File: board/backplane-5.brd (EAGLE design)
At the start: 100 x 100 mm, 155 parts, among them CN1 RJ45JACK90, CN2 4PINCONNFEMALE-1.6, CN3 4PINCONNFEMALE-1.6, CN4 4PINCONNFEMALE-1.6, CN5 4PINCONNFEMALE-1.6, CN6 4PINCONNFEMALE-1.6, U1 AMS1117-5.0, U10 RT9193, U11 KSZ9897, U12 KSZ8081MLX, U13 STM32F217-100, U2 AMS1117-5.0, U3 AMS1117-5.0, U4 AMS1117-5.0, U5 AMS1117-5.0, U6 AMS1117-2.5, U7 AMS1117-1.2, U8 RT9193, U9 AMS1117-5.0, Y1 25MHz, Y2 25MHz, Y3 25MHz

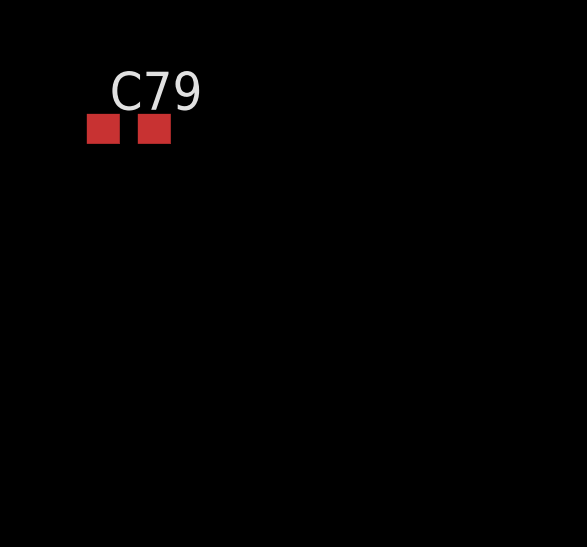
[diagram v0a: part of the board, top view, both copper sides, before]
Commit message: Added VCAP capacitors
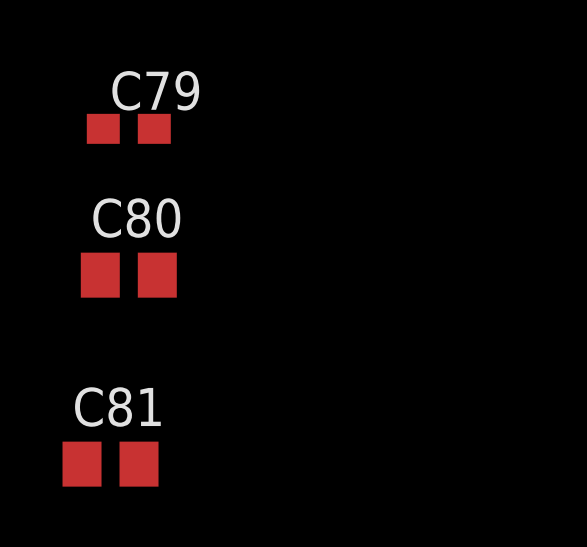
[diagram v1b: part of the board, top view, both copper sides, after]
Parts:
- added C80, C81: 2.2uF, tuetuopay:0805
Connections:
- new net N$34: C80.1, U13.73
- new net N$35: C81.1, U13.49
- net GND: now also C80.2, C81.2
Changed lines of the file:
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@@
 <element name="C78" library="tuetuopay" package="0603" value="10nF" x="-151.1808" y="-580.7456"/>
 <element name="C79" library="tuetuopay" package="0603" value="10nF" x="-151.1808" y="-585.6224"/>
+<element name="C80" library="tuetuopay" package="0805" value="2.2uF" x="-151.1808" y="-590.4992"/>
+<element name="C81" library="tuetuopay" package="0805" value="2.2uF" x="-151.7904" y="-596.7984"/>
 </elements>
 <signals>
@@
 <contactref element="C69" pad="2"/>
 <contactref element="C71" pad="2"/>
-<contactref element="U13" pad="10"/>
-<contactref element="U13" pad="20"/>
-<contactref element="U13" pad="27"/>
-<contactref element="U13" pad="74"/>
 <contactref element="C72" pad="2"/>
 <contactref element="C79" pad="2"/>
@@
 <contactref element="C77" pad="2"/>
 <contactref element="C78" pad="2"/>
+<contactref element="C81" pad="2"/>
+<contactref element="U13" pad="10"/>
+<contactref element="U13" pad="20"/>
+<contactref element="U13" pad="27"/>
+<contactref element="U13" pad="74"/>
+<contactref element="C80" pad="2"/>
 <wire x1="-106.26" y1="-387.35" x2="-106.26" y2="-400.05" width="0" layer="19" extent="1-1"/>
 <wire x1="-106.26" y1="-374.65" x2="-106.26" y2="-387.35" width="0" layer="19" extent="1-1"/>
@@
 <wire x1="-150.3308" y1="-580.7456" x2="-150.3308" y2="-575.8688" width="0" layer="19" extent="1-1"/>
 <wire x1="-150.3308" y1="-585.6224" x2="-150.3308" y2="-580.7456" width="0" layer="19" extent="1-1"/>
+<wire x1="-150.2308" y1="-590.4992" x2="-150.3308" y2="-585.6224" width="0" layer="19" extent="1-1"/>
+<wire x1="-150.8404" y1="-596.7984" x2="-150.2308" y2="-590.4992" width="0" layer="19" extent="1-1"/>
 <wire x1="-76.62" y1="-128.27" x2="-84.24" y2="-219.71" width="0" layer="19" extent="1-1"/>
 <wire x1="12.44" y1="5.83" x2="-76.62" y2="-128.27" width="0" layer="19" extent="1-1"/>
@@
 <wire x1="-137.8792" y1="-534.038" x2="-152.0308" y2="-546.608" width="0" layer="19" extent="1-1"/>
 </signal>
+<signal name="N$34">
+<contactref element="U13" pad="73"/>
+<contactref element="C80" pad="1"/>
+<wire x1="-143.3792" y1="-518.538" x2="-152.1308" y2="-590.4992" width="0" layer="19" extent="1-1"/>
+</signal>
+<signal name="N$35">
+<contactref element="U13" pad="49"/>
+<contactref element="C81" pad="1"/>
+<wire x1="-130.6292" y1="-520.788" x2="-152.7404" y2="-596.7984" width="0" layer="19" extent="1-1"/>
+</signal>
 </signals>

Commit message: Added switch <-> stm32 rmii in schematic
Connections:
- new net STM32-ETH-CRSDV: U11.P$76, U13.32
- new net STM32-ETH-REFCLK: U11.P$66, U13.24
- new net STM32-ETH-RXD0: U11.P$83, U13.33
- new net STM32-ETH-RXD1: U11.P$82, U13.34
- new net STM32-ETH-TXD0: U11.P$73, U13.51
- new net STM32-ETH-TXD1: U11.P$72, U13.52
- new net STM32-ETH-TXEN: U11.P$67, U13.48
- net MDC: now also U13.16
- net MDIO: now also U13.25
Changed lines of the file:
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@@
 <contactref element="U11" pad="P$101"/>
 <contactref element="JP1" pad="2"/>
+<contactref element="U13" pad="16"/>
+<wire x1="-137.16" y1="-509.27" x2="-136.8792" y2="-534.038" width="0" layer="19" extent="1-1"/>
 <wire x1="31.9492" y1="22.5724" x2="-137.16" y2="-509.27" width="0" layer="19" extent="1-1"/>
 <wire x1="66.528" y1="24.6608" x2="31.9492" y2="22.5724" width="0" layer="19" extent="1-1"/>
@@
 <wire x1="31.4492" y1="22.5724" x2="31.4492" y2="20.2008" width="0.2032" layer="1"/>
 <wire x1="31.4492" y1="20.2008" x2="31.6992" y2="19.9508" width="0.2032" layer="1"/>
+<contactref element="U13" pad="25"/>
+<wire x1="-139.7" y1="-509.27" x2="-132.3792" y2="-534.038" width="0" layer="19" extent="1-1"/>
 <wire x1="31.6992" y1="19.9508" x2="-139.7" y2="-509.27" width="0" layer="19" extent="1-1"/>
 <wire x1="66.528" y1="23.4608" x2="31.6992" y2="19.9508" width="0" layer="19" extent="1-1"/>
@@
 <wire x1="-130.6292" y1="-520.788" x2="-152.7404" y2="-596.7984" width="0" layer="19" extent="1-1"/>
 </signal>
+<signal name="STM32-ETH-REFCLK">
+<contactref element="U13" pad="24"/>
+<contactref element="U11" pad="P$66"/>
+<wire x1="53.128" y1="22.0608" x2="-132.8792" y2="-534.038" width="0" layer="19" extent="1-1"/>
+</signal>
+<signal name="STM32-ETH-CRSDV">
+<contactref element="U13" pad="32"/>
+<contactref element="U11" pad="P$76"/>
+<wire x1="57.128" y1="22.0608" x2="-130.6292" y2="-529.288" width="0" layer="19" extent="1-1"/>
+</signal>
+<signal name="STM32-ETH-RXD0">
+<contactref element="U13" pad="33"/>
+<contactref element="U11" pad="P$83"/>
+<wire x1="59.928" y1="22.0608" x2="-130.6292" y2="-528.788" width="0" layer="19" extent="1-1"/>
+</signal>
+<signal name="STM32-ETH-RXD1">
+<contactref element="U13" pad="34"/>
+<contactref element="U11" pad="P$82"/>
+<wire x1="59.528" y1="22.0608" x2="-130.6292" y2="-528.288" width="0" layer="19" extent="1-1"/>
+</signal>
+<signal name="STM32-ETH-TXEN">
+<contactref element="U13" pad="48"/>
+<contactref element="U11" pad="P$67"/>
+<wire x1="53.528" y1="22.0608" x2="-130.6292" y2="-521.288" width="0" layer="19" extent="1-1"/>
+</signal>
+<signal name="STM32-ETH-TXD0">
+<contactref element="U13" pad="51"/>
+<contactref element="U11" pad="P$73"/>
+<wire x1="55.928" y1="22.0608" x2="-132.3792" y2="-518.538" width="0" layer="19" extent="1-1"/>
+</signal>
+<signal name="STM32-ETH-TXD1">
+<contactref element="U13" pad="52"/>
+<contactref element="U11" pad="P$72"/>
+<wire x1="55.528" y1="22.0608" x2="-132.8792" y2="-518.538" width="0" layer="19" extent="1-1"/>
+</signal>
 </signals>

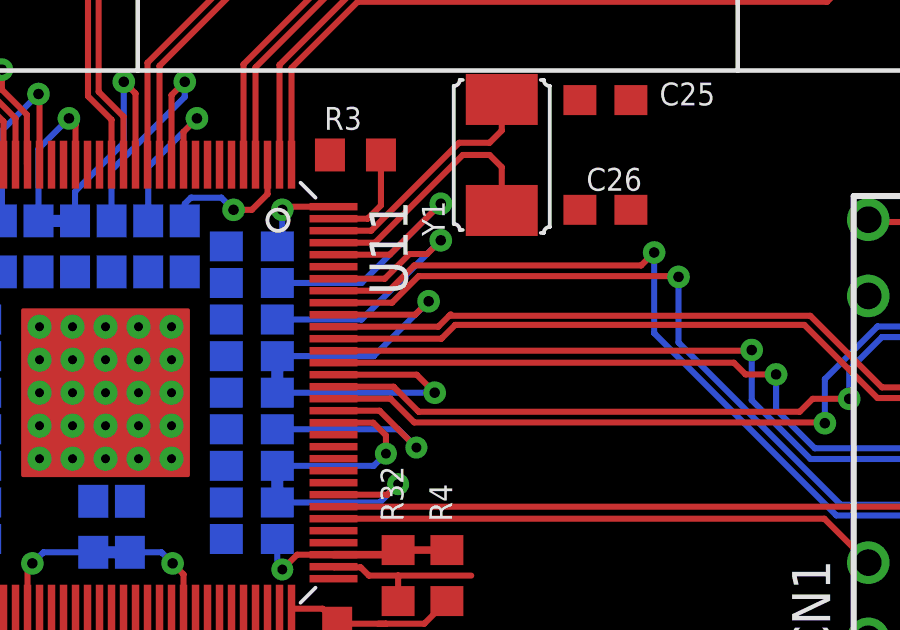
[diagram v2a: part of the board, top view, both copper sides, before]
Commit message: Added the REFCLK source for switch <-> stm
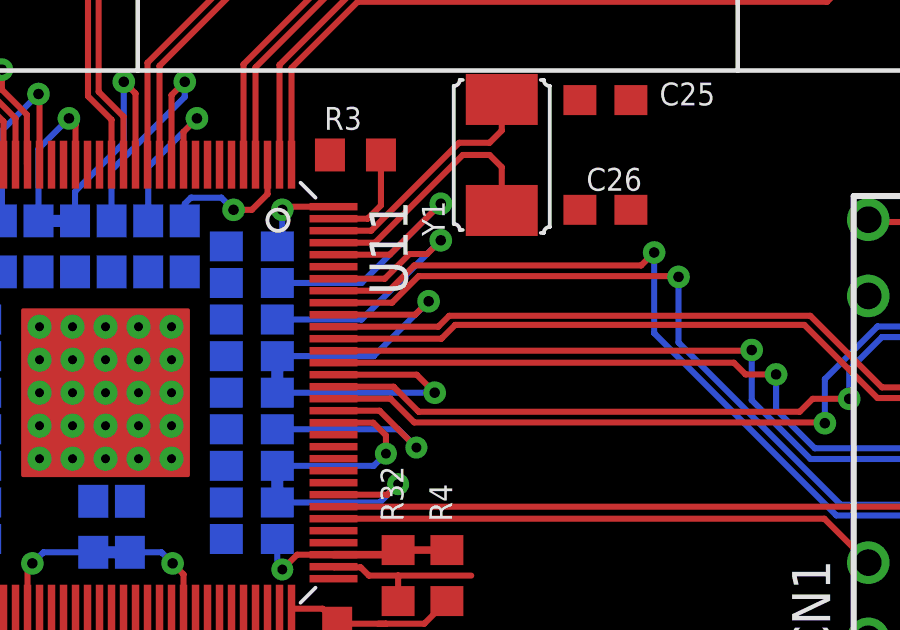
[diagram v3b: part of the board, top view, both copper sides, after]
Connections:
- net STM32-ETH-REFCLK: now also U13.67
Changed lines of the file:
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@@
 <layer number="27" name="tValues" color="7" fill="1" visible="yes" active="yes"/>
 <layer number="28" name="bValues" color="7" fill="1" visible="yes" active="yes"/>
-<layer number="29" name="tStop" color="7" fill="3" visible="no" active="yes"/>
-<layer number="30" name="bStop" color="7" fill="6" visible="no" active="yes"/>
+<layer number="29" name="tStop" color="7" fill="3" visible="yes" active="yes"/>
+<layer number="30" name="bStop" color="7" fill="6" visible="yes" active="yes"/>
 <layer number="31" name="tCream" color="7" fill="4" visible="no" active="yes"/>
 <layer number="32" name="bCream" color="7" fill="5" visible="no" active="yes"/>
@@
 <wire x1="33.528" y1="15.8124" x2="-76.07" y2="-123.19" width="0" layer="19" extent="1-1"/>
 <wire x1="35.1536" y1="15.8124" x2="33.528" y2="15.8124" width="0" layer="19" extent="1-1"/>
+<wire x1="31.6992" y1="18.2508" x2="33.528" y2="15.8124" width="0" layer="19" extent="1-1"/>
 <wire x1="38.608" y1="16.0156" x2="35.1536" y2="15.8124" width="0" layer="19" extent="1-1"/>
-<wire x1="31.6992" y1="18.2508" x2="33.528" y2="15.8124" width="0" layer="19" extent="1-1"/>
 <wire x1="35.9492" y1="24.0724" x2="31.6992" y2="18.2508" width="0" layer="19" extent="1-1"/>
 <wire x1="48.1584" y1="23.5712" x2="39.8272" y2="23.6084" width="0" layer="19" extent="1-1"/>
@@
 <wire x1="66.528" y1="31.4608" x2="70.02055" y2="31.4608" width="0.2032" layer="1"/>
 <wire x1="70.02055" y1="31.4608" x2="70.384675" y2="31.824925" width="0.2032" layer="1"/>
-<wire x1="70.384675" y1="31.824925" x2="70.43675" y2="31.877" width="0.2032" layer="1"/>
 <wire x1="70.384675" y1="31.824925" x2="82.421725" y2="31.824925" width="0.2032" layer="1"/>
 <wire x1="82.421725" y1="31.824925" x2="84.80805" y2="29.4386" width="0.2032" layer="1"/>
@@
 <contactref element="U13" pad="24"/>
 <contactref element="U11" pad="P$66"/>
-<wire x1="53.128" y1="22.0608" x2="-132.8792" y2="-534.038" width="0" layer="19" extent="1-1"/>
+<contactref element="U13" pad="67"/>
+<wire x1="-140.3792" y1="-518.538" x2="-132.8792" y2="-534.038" width="0" layer="19" extent="1-1"/>
+<wire x1="53.128" y1="22.0608" x2="-140.3792" y2="-518.538" width="0" layer="19" extent="1-1"/>
 </signal>
 <signal name="STM32-ETH-CRSDV">

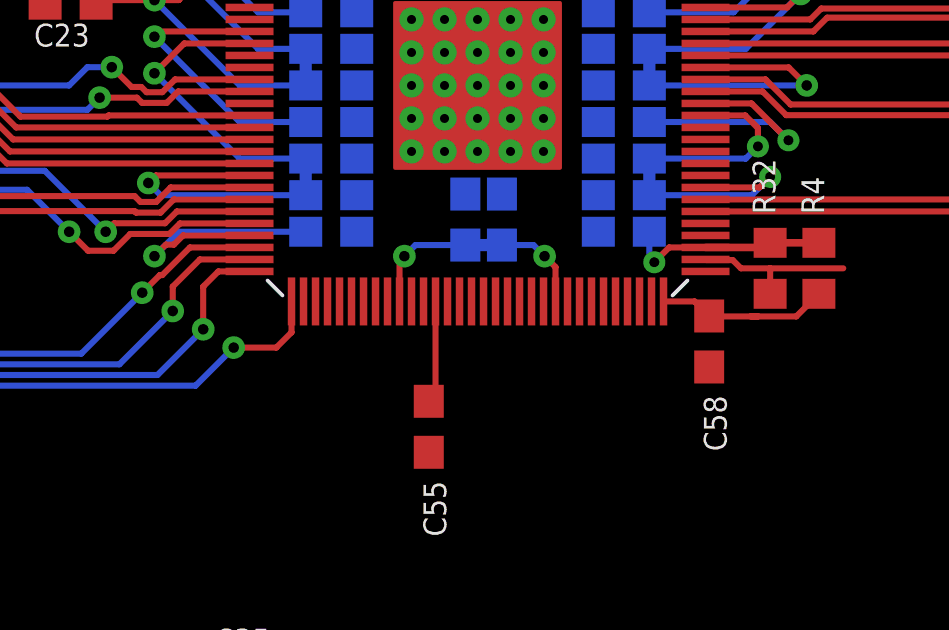
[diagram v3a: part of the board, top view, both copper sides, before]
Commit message: Proper supply symbols for some supply rails
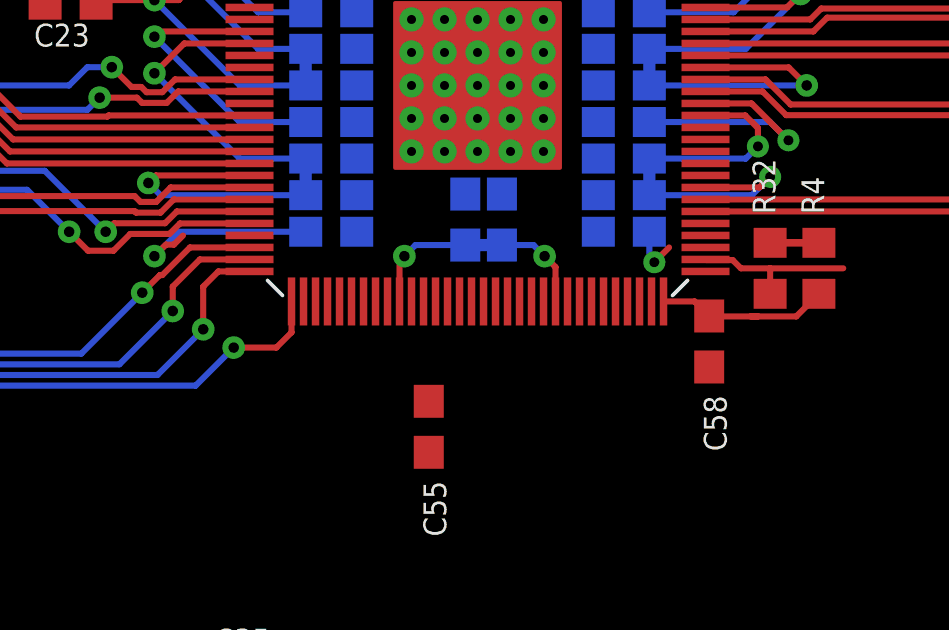
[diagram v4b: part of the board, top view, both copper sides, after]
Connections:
- net 12V renamed +12V
- net 5V renamed +5V
- removed net 2V5: C11.P, C54.1, C55.1, C56.1, C57.1, C61.1, C62.1, L2.2, LED1.A, LED10.A, LED2.A, LED3.A, LED4.A, LED5.A, LED6.A, LED7.A, LED8.A, LED9.A, R16.2, R29.1, R30.1, R31.1, R32.2, R4.2, R7.2, R8.2, U11.P$61, U11.P$77, U11.P$99, U12.25, U6.2
- new net VCCIO: C11.P, C54.1, C55.1, C56.1, C57.1, C61.1, C62.1, C72.1, C73.1, C74.1, C75.1, C76.1, C77.1, C78.1, C79.1, L2.2, LED1.A, LED10.A, LED2.A, LED3.A, LED4.A, LED5.A, LED6.A, LED7.A, LED8.A, LED9.A, R16.2, R29.1, R30.1, R31.1, R32.2, R4.2, R6.2, R7.2, R8.2, U11.P$61, U11.P$77, U11.P$99, U12.25, U13.100, U13.11, U13.19, U13.21, U13.22, U13.28, U13.50, U13.75, U6.2
- net 3V3-PHY: no longer R6.2
- net 3V3-STM32: no longer C72.1, C73.1, C74.1, C75.1, C76.1, C77.1, C78.1, C79.1, U13.100, U13.11, U13.19, U13.21, U13.22, U13.28, U13.50, U13.75
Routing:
- net 2V5: track 23.2 -> 0.00 mm, vias 2 -> 0
- net VCCIO: track 0.00 -> 14.7 mm, vias 0 -> 2
